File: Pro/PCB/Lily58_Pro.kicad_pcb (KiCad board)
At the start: 2 copper layers, 142.5 x 106.3 mm, 87 parts, among them J1 LED, J2 4PIN, J3 OLED, P1 i2c_pin, P2 i2c_pin, SW1 SW_PUSH, SW10 SW_PUSH, SW11 SW_PUSH, SW12 SW_PUSH, SW13 SW_PUSH, SW14 SW_PUSH, SW15 SW_PUSH, SW16 SW_PUSH, SW17 SW_PUSH, SW18 SW_PUSH, SW19 SW_PUSH, SW2 SW_PUSH, SW20 SW_PUSH, SW21 SW_PUSH, SW22 SW_PUSH, SW23 SW_PUSH, SW24 SW_PUSH, SW25 SW_PUSH, SW26 SW_PUSH, SW27 SW_PUSH, SW28 SW_PUSH, SW29 SW_PUSH, SW3 SW_PUSH, SW4 SW_PUSH, SW5 SW_PUSH, SW6 SW_PUSH, SW7 SW_PUSH, SW8 SW_PUSH, SW9 SW_PUSH, U1 ProMicro

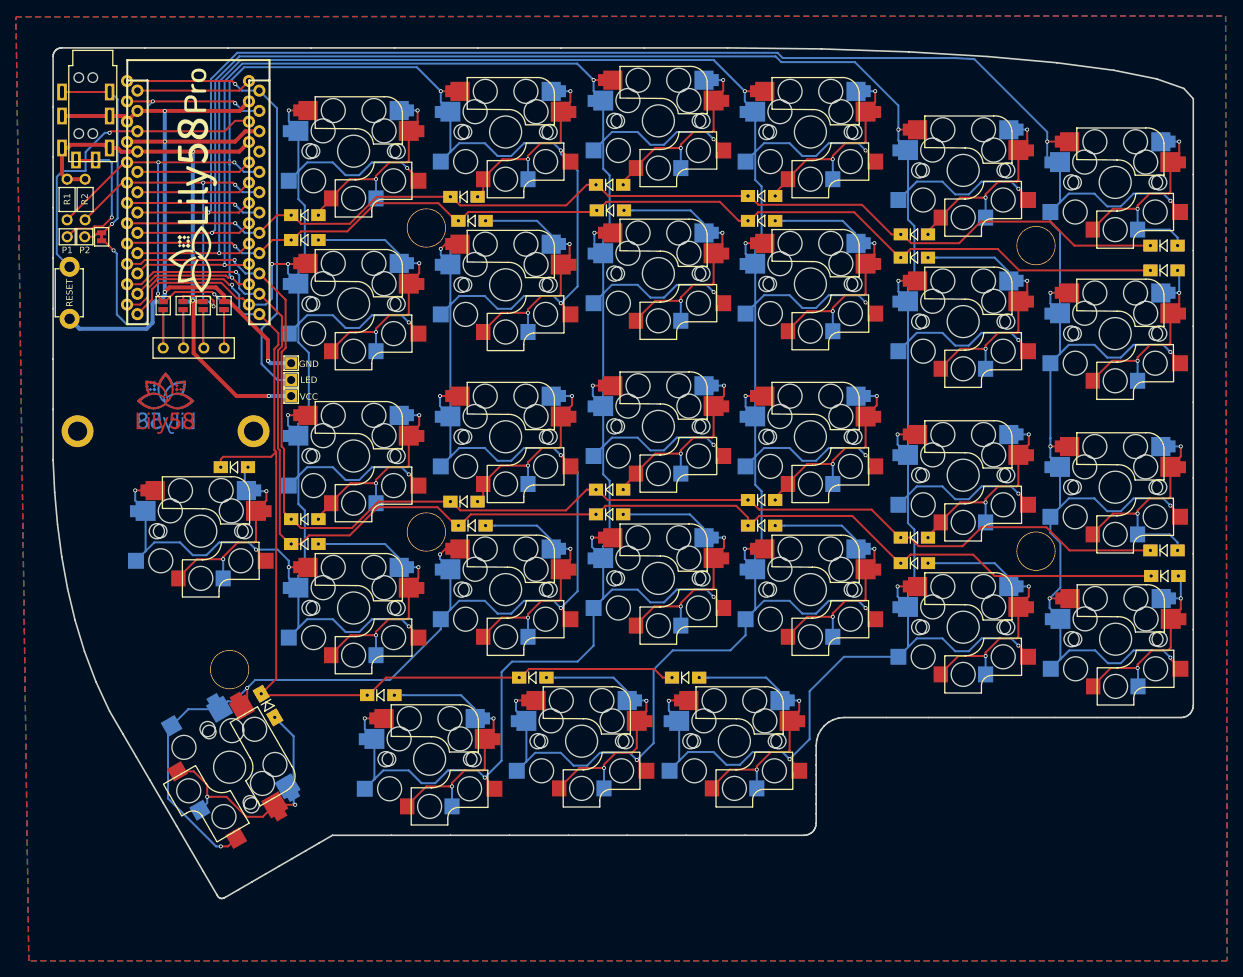
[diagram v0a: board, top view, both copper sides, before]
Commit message: Added power switch and JST-PH 2.0 connector for battery. Flooded islands and via stitched top and bottom ground planes.
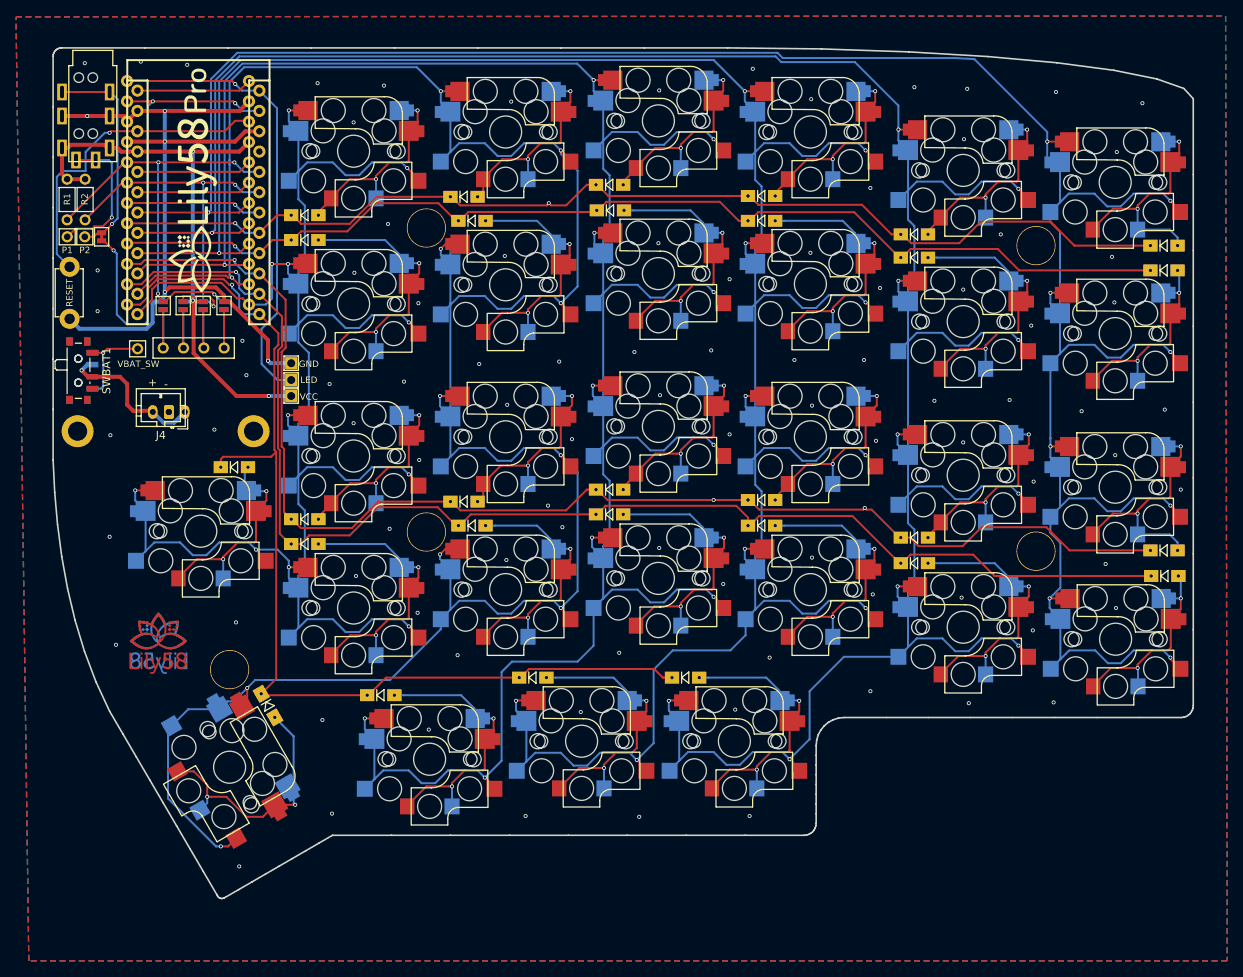
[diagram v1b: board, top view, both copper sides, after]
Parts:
- added J4: Conn_01x02, Connector_JST:JST_PH_B2B-PH-K_1x02_P2.00mm_Vertical, F.Cu at (97.4, 82.6)
- added J5: Conn_01x02, Connector_JST:JST_PH_B2B-PH-K_1x02_P2.00mm_Vertical, B.Cu at (97.4, 82.6)
- added P5: VBAT_SW, Lily58_Pro-footprint:1pin_conn, F.Cu at (93.5, 74.7)
- added SWBAT1: SW_SPDT, Button_Switch_SMD:SW_SPDT_PCM12, F.Cu at (86.4, 77.5)
- added SWBAT2: SW_SPDT, Button_Switch_SMD:SW_SPDT_PCM12, B.Cu at (86.4, 77.4)
- moved G*** 30.0 mm to (96.1, 111.5) (x2)
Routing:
- net Net-(J4-Pin_2): track 0.00 -> 19.3 mm, vias 0 -> 1
- net Net-(P5-Pin_1): track 0.00 -> 11.9 mm, vias 0 -> 1
- net row0: track 138.2 -> 138.4 mm, vias 1 -> 2
- net row2: track 166.3 -> 166.4 mm, vias 1 -> 3
- net GND: vias 4 -> 97
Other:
- board text added: "+"
- board text added: "-"

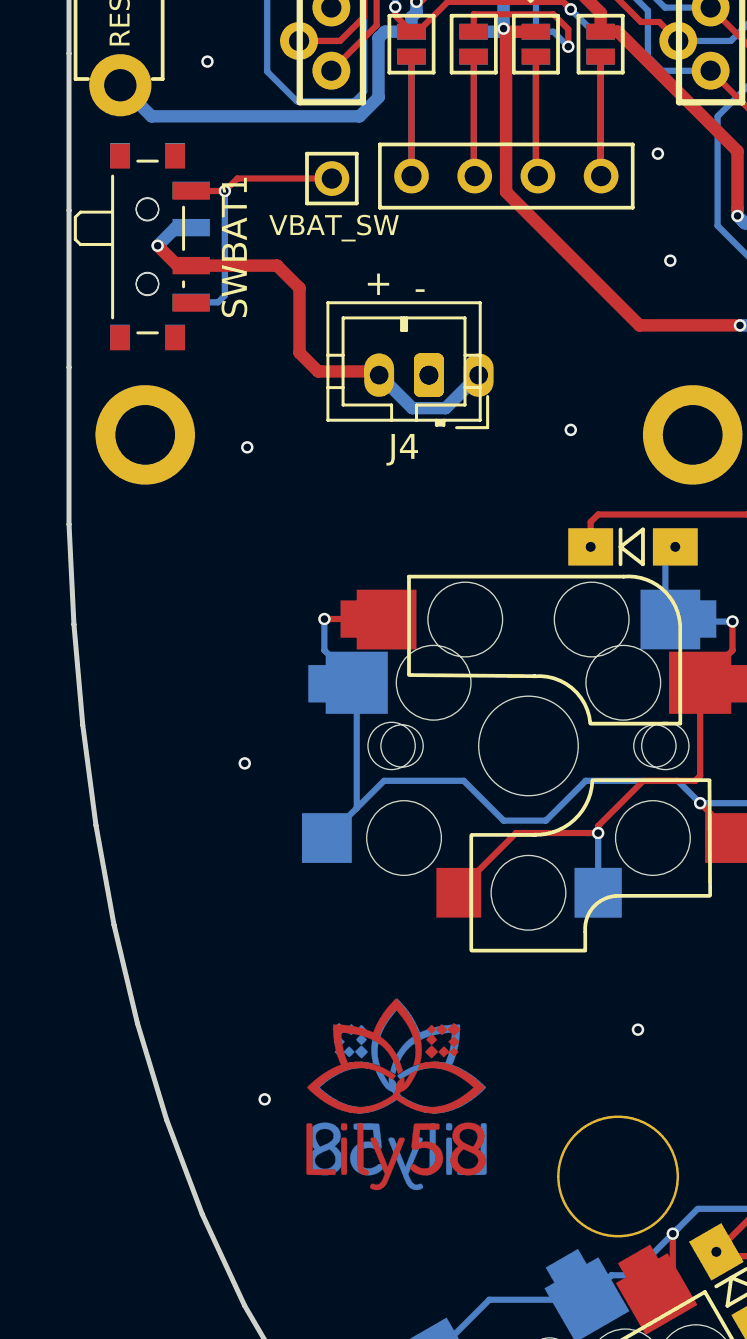
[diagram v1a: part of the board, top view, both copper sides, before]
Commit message: Added "feat. CamS" as logo on copper layer
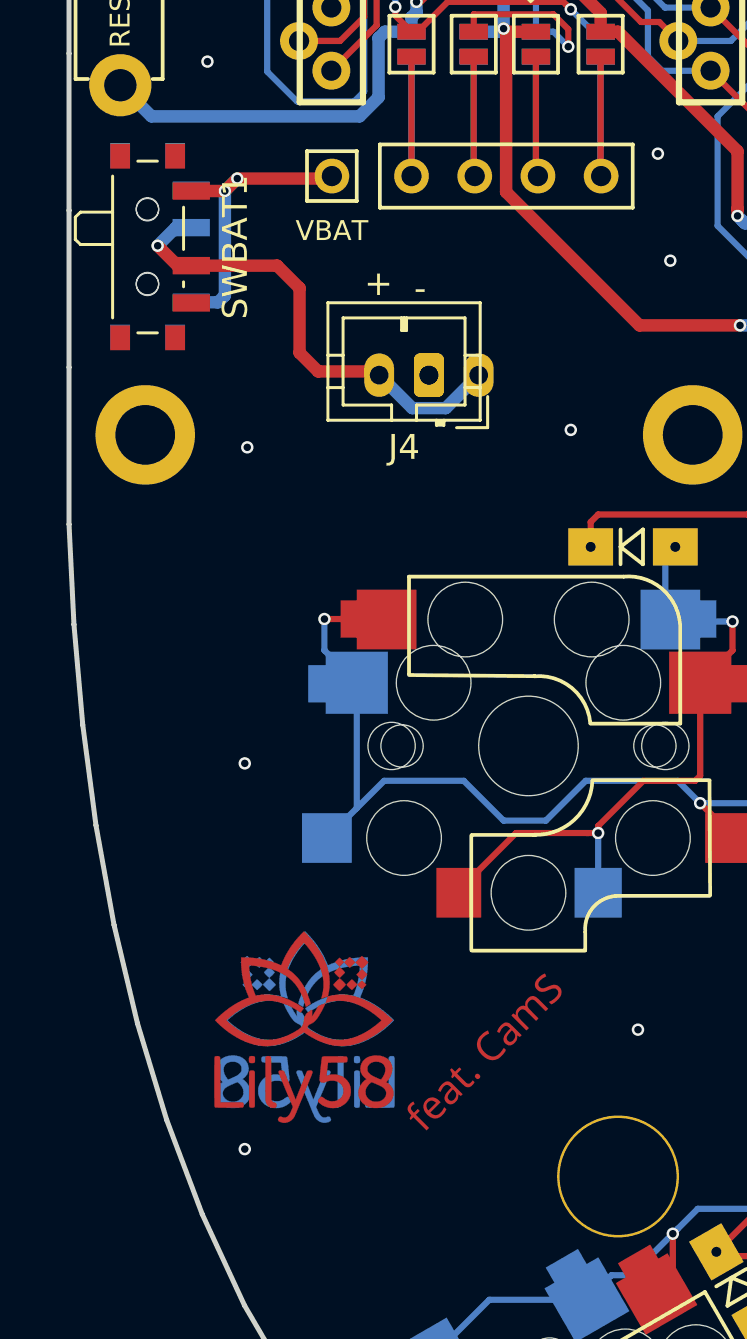
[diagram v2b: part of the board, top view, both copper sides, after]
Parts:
- added G***: LOGO, Attabotics:featCamS_8mm, F.Cu at (99.6, 109.8)
- P5: value VBAT_SW -> VBAT
- moved G*** 4.58 mm to (92.4, 108.8) (x2)
- moved P5 0.10 mm to (93.5, 74.6)
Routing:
- net Net-(P5-Pin_1): track 11.9 -> 12.6 mm, vias 1 -> 2

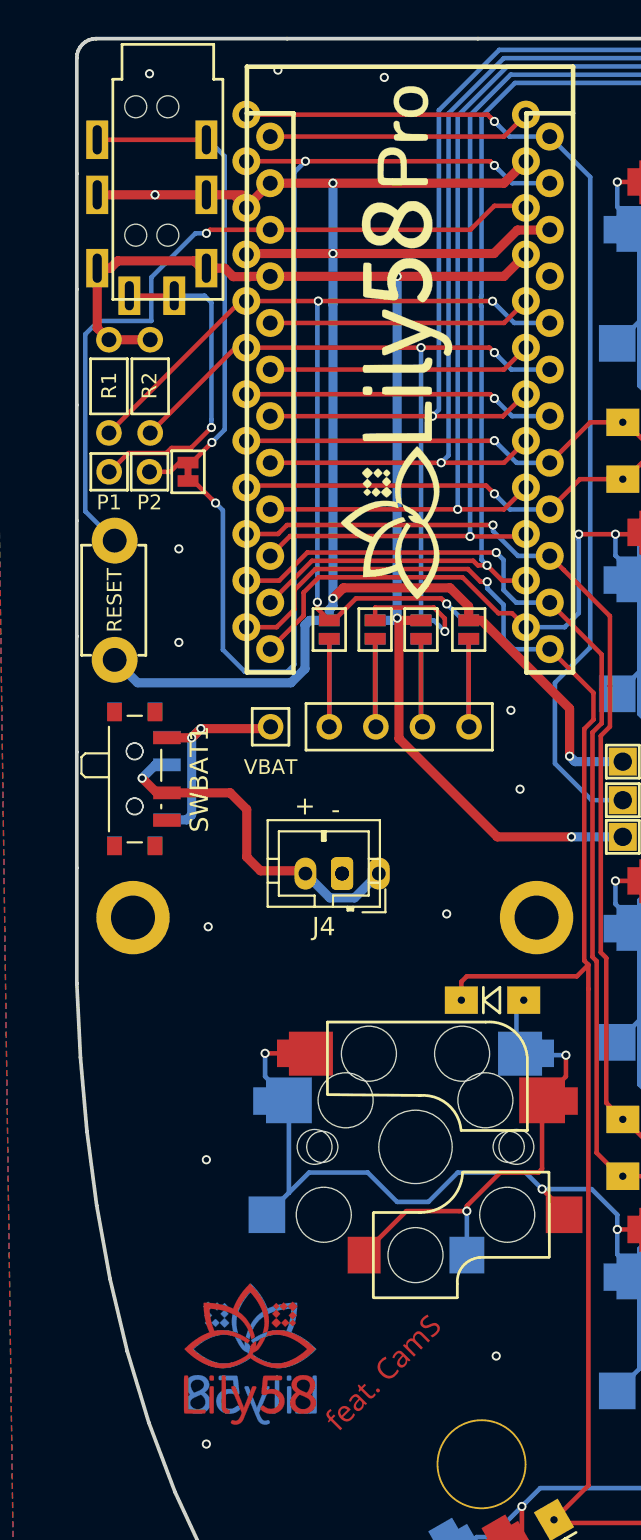
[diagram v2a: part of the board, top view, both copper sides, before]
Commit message: Added connection from VBAT_SW to RAW pin on nano socket (for Nice!Nano)
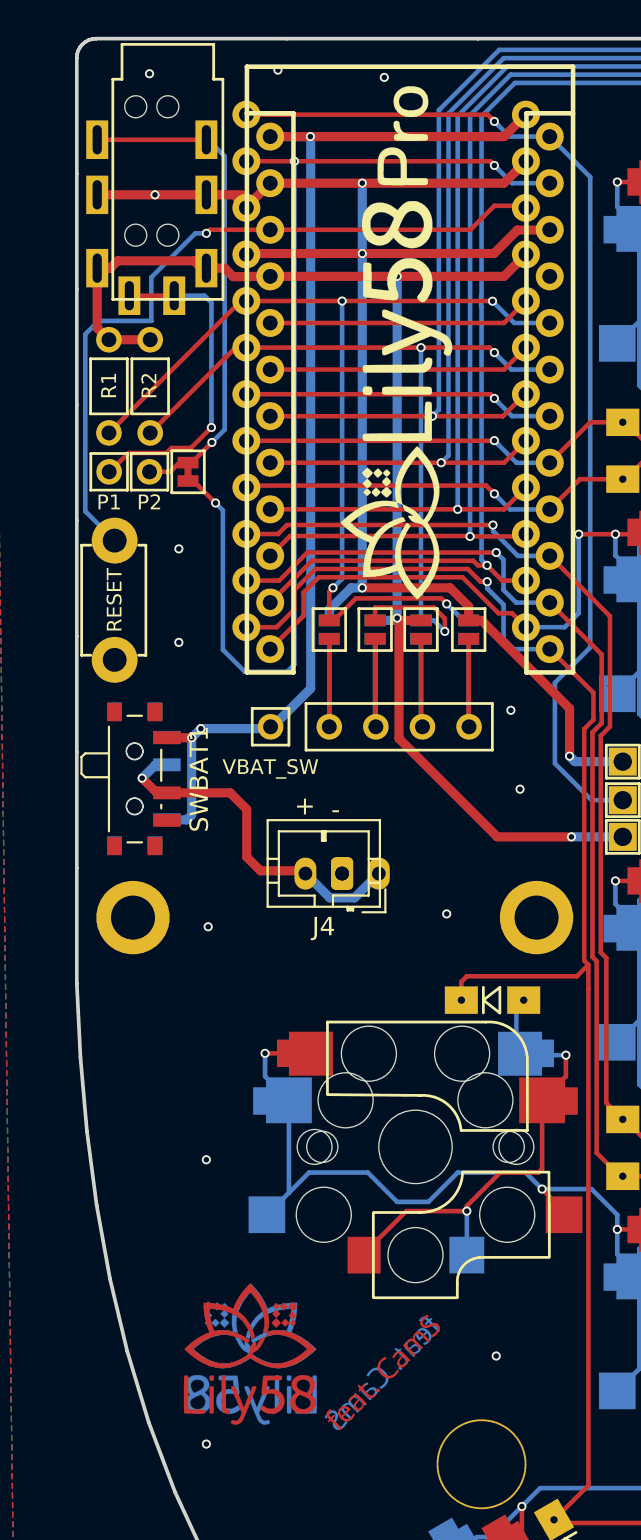
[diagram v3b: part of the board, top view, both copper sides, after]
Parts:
- added G***: LOGO, Attabotics:featCamS_8mm, B.Cu at (99.6, 109.8)
- P5: value VBAT -> VBAT_SW
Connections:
- P5 pad 1: Net-(P5-Pin_1) -> VBAT_SW
- SWBAT1 pad 1: Net-(P5-Pin_1) -> VBAT_SW
- SWBAT2 pad 1: Net-(P5-Pin_1) -> VBAT_SW
- U1 pad 24: unconnected-(U1-RAW-Pad24) -> VBAT_SW
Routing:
- net VBAT_SW: track 0.00 -> 61.7 mm, vias 0 -> 3
- net GND: track 102.8 -> 87.0 mm
- net unconnected-(U1-RAW-Pad24): track 14.4 -> 0.00 mm
- net Net-(P5-Pin_1): track 12.6 -> 0.00 mm, vias 2 -> 0
- net DATA: track 60.1 -> 59.2 mm

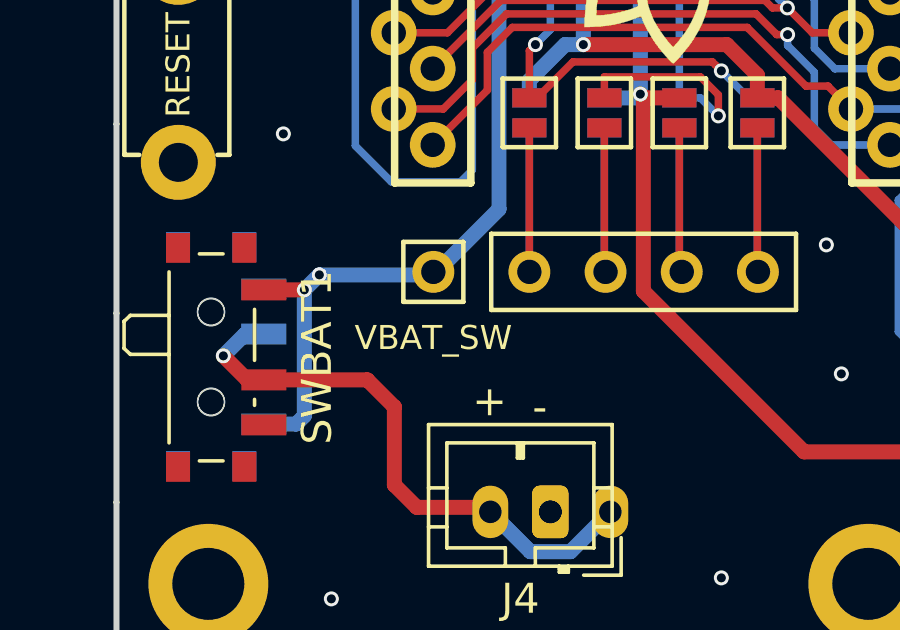
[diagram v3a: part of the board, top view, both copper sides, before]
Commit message: Minor cosmetic updates to PCB
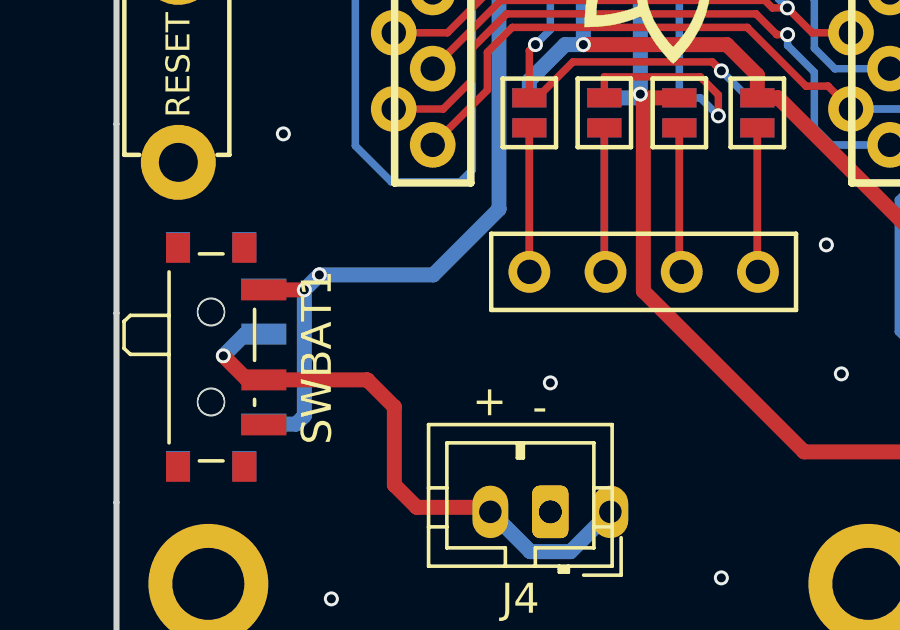
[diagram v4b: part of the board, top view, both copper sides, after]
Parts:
- removed P5: VBAT_SW, Lily58_Pro-footprint:1pin_conn
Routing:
- net GND: vias 97 -> 98
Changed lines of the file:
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@@
       (stroke (width 0.01) (type solid)) (fill solid) (layer "F.Cu"))
   )
-  (footprint "Lily58_Pro-footprint:1pin_conn" (layer "F.Cu")
-    (at 93.5 74.6 180)
-    (descr "Resitance 3 pas")
-    (tags "R")
-    (property "Sheetfile" "Lily58_Pro.kicad_sch")
-    (property "Sheetname" "")
-    (attr through_hole)
-    (fp_text reference "P5" (at 1.9 0.1) (layer "F.SilkS") hide
-        (effects (font (size 0.8128 0.8128) (thickness 0.15)))
-    )
-    (fp_text value "VBAT_SW" (at 0 -2.2) (layer "F.SilkS")
-        (effects (font (size 0.8 0.8) (thickness 0.15)))
-    )
-    (fp_text user "P5" (at 1.8 0.1) (layer "B.SilkS") hide
-        (effects (font (size 0.8128 0.8128) (thickness 0.15)) (justify mirror))
-    )
-    (fp_text user "VBAT" (at 0 -2.2 unlocked) (layer "B.SilkS")
-        (effects (font (size 0.8 0.8) (thickness 0.15)) (justify mirror))
-    )
-    (fp_line (start -1 -1) (end 1 -1)
-      (stroke (width 0.15) (type solid)) (layer "B.SilkS"))
-    (fp_line (start -1 1) (end -1 -1)
-      (stroke (width 0.15) (type solid)) (layer "B.SilkS"))
-    (fp_line (start 1 -1) (end 1 1)
-      (stroke (width 0.15) (type solid)) (layer "B.SilkS"))
-    (fp_line (start 1 1) (end -1 1)
-      (stroke (width 0.15) (type solid)) (layer "B.SilkS"))
-    (fp_line (start -1 -1) (end -1 1)
-      (stroke (width 0.15) (type solid)) (layer "F.SilkS"))
-    (fp_line (start -1 1) (end 1 1)
-      (stroke (width 0.15) (type solid)) (layer "F.SilkS"))
-    (fp_line (start 1 -1) (end -1 -1)
-      (stroke (width 0.15) (type solid)) (layer "F.SilkS"))
-    (fp_line (start 1 1) (end 1 -1)
-      (stroke (width 0.15) (type solid)) (layer "F.SilkS"))
-    (pad "1" thru_hole circle (at 0 0 180) (size 1.397 1.397) (drill 0.8128) (layers "*.Cu" "*.Mask" "F.SilkS")
-      (net 57 "VBAT_SW") (pinfunction "Pin_1") (pintype "passive"))
-    (model "discret/resistor.wrl"
-      (offset (xyz 0 0 0))
-      (scale (xyz 0.3 0.3 0.3))
-      (rotate (xyz 0 0 0))
-    )
-    (model "Resistors_ThroughHole.3dshapes/Resistor_Horizontal_RM10mm.wrl"
-      (offset (xyz 0 0 0))
-      (scale (xyz 0.2 0.2 0.2))
-      (rotate (xyz 0 0 0))
-    )
-  )
   (footprint "Button_Switch_SMD:SW_SPDT_PCM12" (layer "F.Cu")
     (at 86.42 77.45 -90)
@@
   (via (at 120.5 84) (size 0.5) (drill 0.3) (layers "F.Cu" "B.Cu") (free) (net 7))
   (via (at 208 118.9) (size 0.5) (drill 0.3) (layers "F.Cu" "B.Cu") (free) (net 7))
+  (via (at 97.4 78.3) (size 0.5) (drill 0.3) (layers "F.Cu" "B.Cu") (free) (net 7))
   (via (at 201.4 60.4) (size 0.5) (drill 0.3) (layers "F.Cu" "B.Cu") (free) (net 7))
   (via (at 88.5 70) (size 0.5) (drill 0.3) (layers "F.Cu" "B.Cu") (free) (net 7))
@@
   (via (at 95.668262 42.427093) (size 0.5) (drill 0.3) (layers "F.Cu" "B.Cu") (net 57))
   (segment (start 95.688 42.512) (end 95.7 42.5) (width 0.5) (layer "B.Cu") (net 57))
-  (segment (start 93.5 74.7) (end 93.5 74.8) (width 0.25) (layer "B.Cu") (net 57))
   (segment (start 95.7 42.5) (end 95.625745 42.425745) (width 0.5) (layer "B.Cu") (net 57))
   (segment (start 89.2 75.2) (end 89.2 79.4) (width 0.5) (layer "B.Cu") (net 57))
   (segment (start 89.2 79.4) (end 88.927163 79.672837) (width 0.5) (layer "B.Cu") (net 57))
-  (segment (start 93.5 74.8) (end 93.3 75) (width 0.25) (layer "B.Cu") (net 57))
   (segment (start 93.5 74.7) (end 95.688 72.512) (width 0.5) (layer "B.Cu") (net 57))
   (segment (start 95.625745 42.425745) (end 93.478815 42.425745) (width 0.5) (layer "B.Cu") (net 57))

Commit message: KiCad 8.0 as ordered 2024-05-22 20:50
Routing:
- net VBAT_SW: vias 3 -> 2
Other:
- outline, holes or cut-outs redrawn
